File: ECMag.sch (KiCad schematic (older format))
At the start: 43 parts, among them J1 Conn_01x12, J2 Conn_01x05, J3 Conn_01x04, J4 USB_B, J5 Barrel_Jack_SW, J6 Conn_01x04, K1 Tactil Switch B3F NA, K2 Tactil Switch B3F NA, K3 Tactil Switch B3F NA, K4 Tactil Switch B3F NA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

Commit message: Rediseño de fuente step up 5v-12v y Actualizacion de datasheets
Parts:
- removed U3: XL6009, Package_TO_SOT_SMD:TO-263-5_TabPin6, symbol Enc_Mag:XL6009
- added R9: 2K2 1%, Resistor_THT:R_Axial_DIN0207_L6.3mm_D2.5mm_P7.62mm_Horizontal, symbol Enc_Mag:Resistencia
- added U3: LM2577, Package_TO_SOT_THT:TO-220-5_P3.4x3.7mm_StaggerOdd_Lead3.8mm_Vertical, symbol Enc_Mag:LM2577
- C2: value 100nF Cerámico -> 330nF Cerámico
- P1: value 10K -> 25K
- R1: value 330 1% -> 2K 1%
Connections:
- net labels added: a1, a10, a2, a3, a4, a5, a6, a7, a8, a9
- wire segments 162 -> 172
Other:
- moved on the sheet: C1, C2

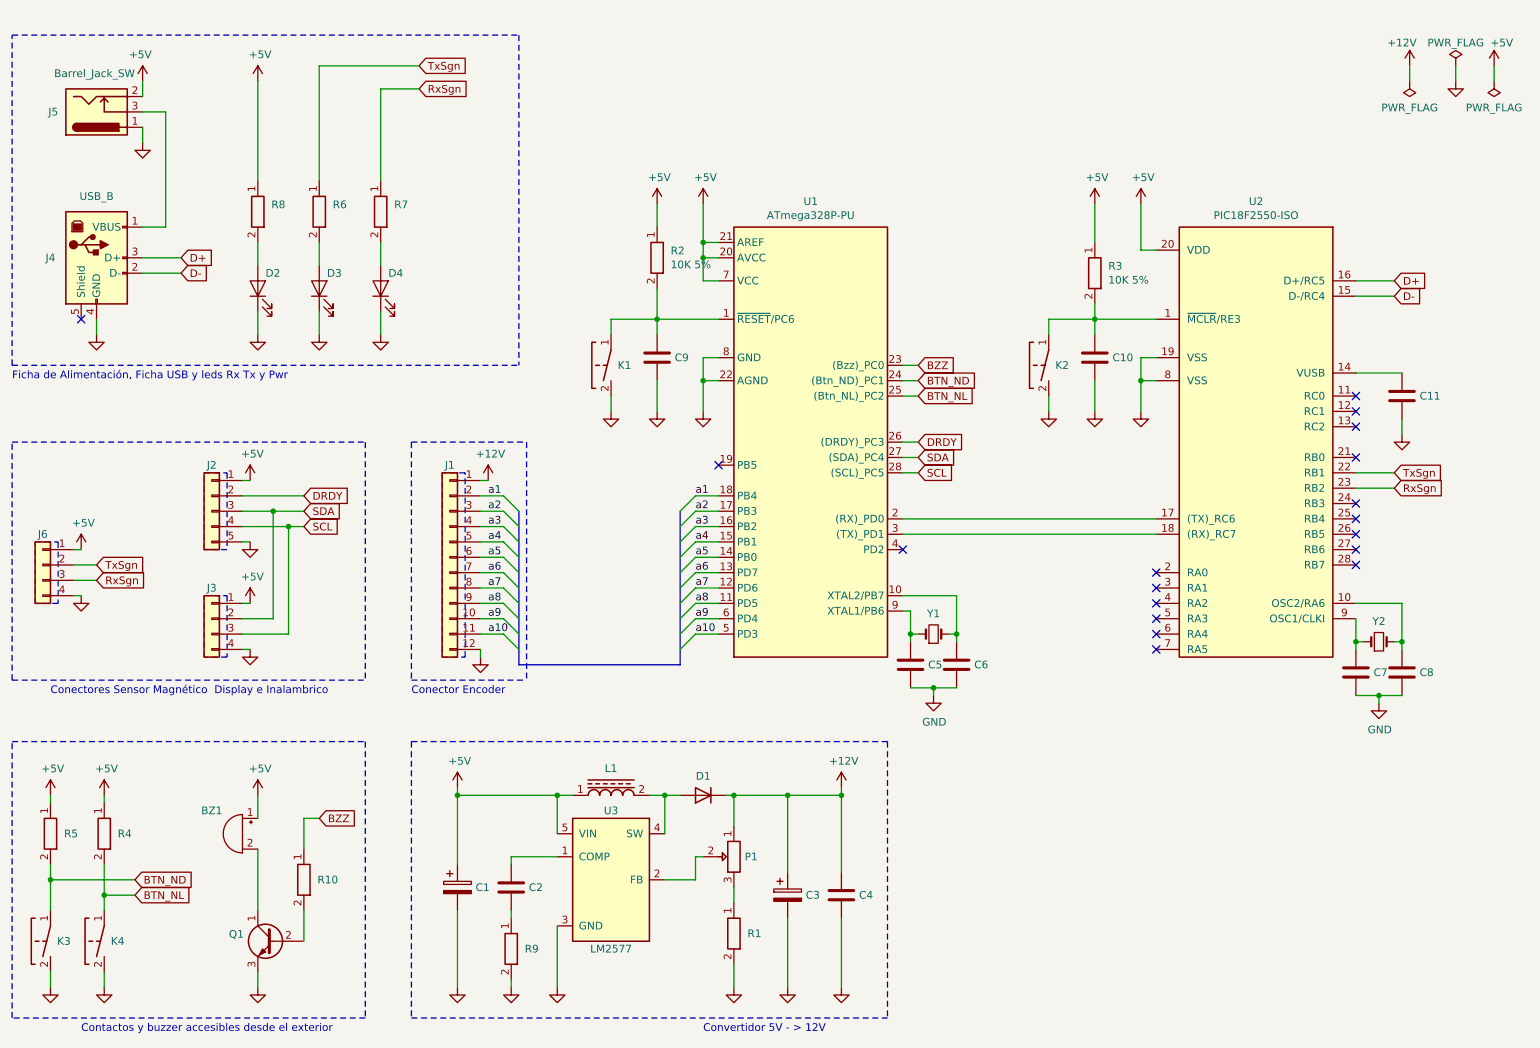
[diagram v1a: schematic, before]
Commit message: compleción de huellas faltantes y reemplazo de etiquetas por buses
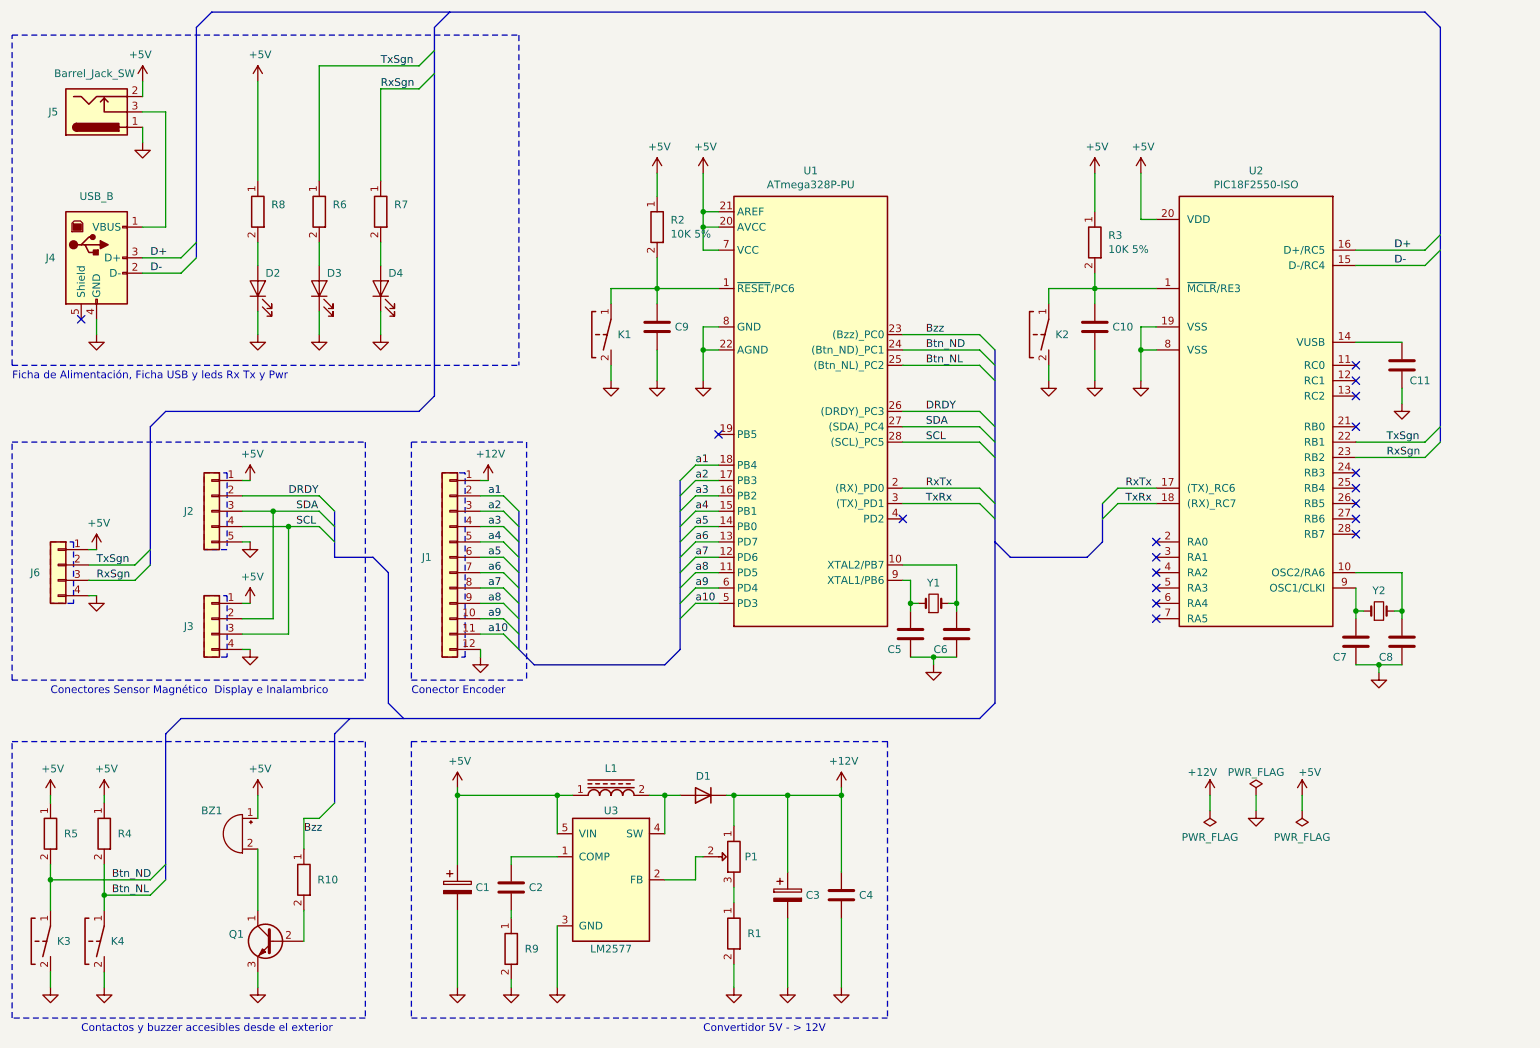
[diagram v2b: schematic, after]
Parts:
- J1: footprint (none) -> Connector_PinHeader_1.27mm:PinHeader_1x12_P1.27mm_Vertical
- J2: footprint (none) -> Connector_PinHeader_1.27mm:PinHeader_1x05_P1.27mm_Vertical
- J3, J6: footprint (none) -> Connector_PinHeader_1.27mm:PinHeader_1x04_P1.27mm_Vertical
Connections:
- net RxTx: now reaches U1.2 ((RX)_PD0), U2.17 ((TX)_RC6)
- net TxRx: now reaches U1.3 ((TX)_PD1), U2.18 ((RX)_RC7)
- net BTN_ND renamed Btn_ND
- net BTN_NL renamed Btn_NL
- net BZZ renamed Bzz
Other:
- moved on the sheet: C10, C11, C5, C6, C7, C8, C9, J6, K1, K2, R2, R3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

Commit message: Inicio de PCB
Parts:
- added H1, H2, H3, H4: MountingHole, MountingHole:MountingHole_3.2mm_M3, symbol Mechanical:MountingHole
- D1: footprint Diode_THT:D_DO-27_P15.24mm_Horizontal -> Diode_THT:D_A-405_P10.16mm_Horizontal
- U2: footprint Package_SO:SOIC-28W_7.5x17.9mm_P1.27mm -> Package_DIP:DIP-28_W7.62mm
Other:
- moved on the sheet: C10, C11, C7, C8, K2, R3, U2, Y2

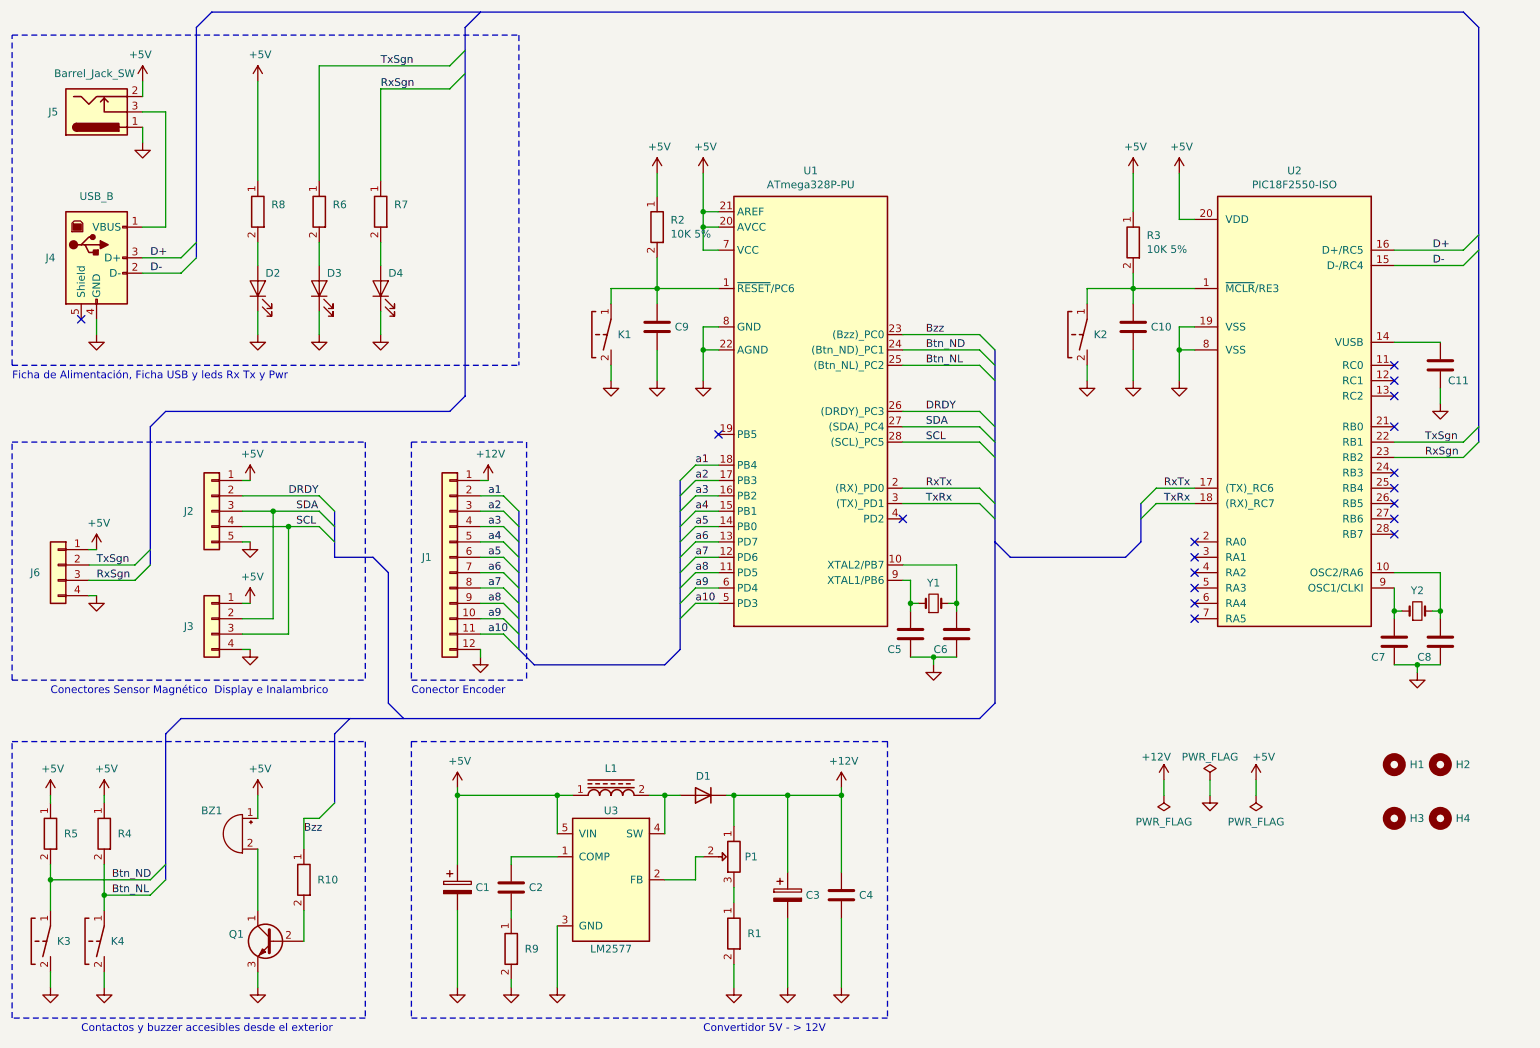
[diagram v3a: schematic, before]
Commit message: agregado de valores de los componentes en el esquemático
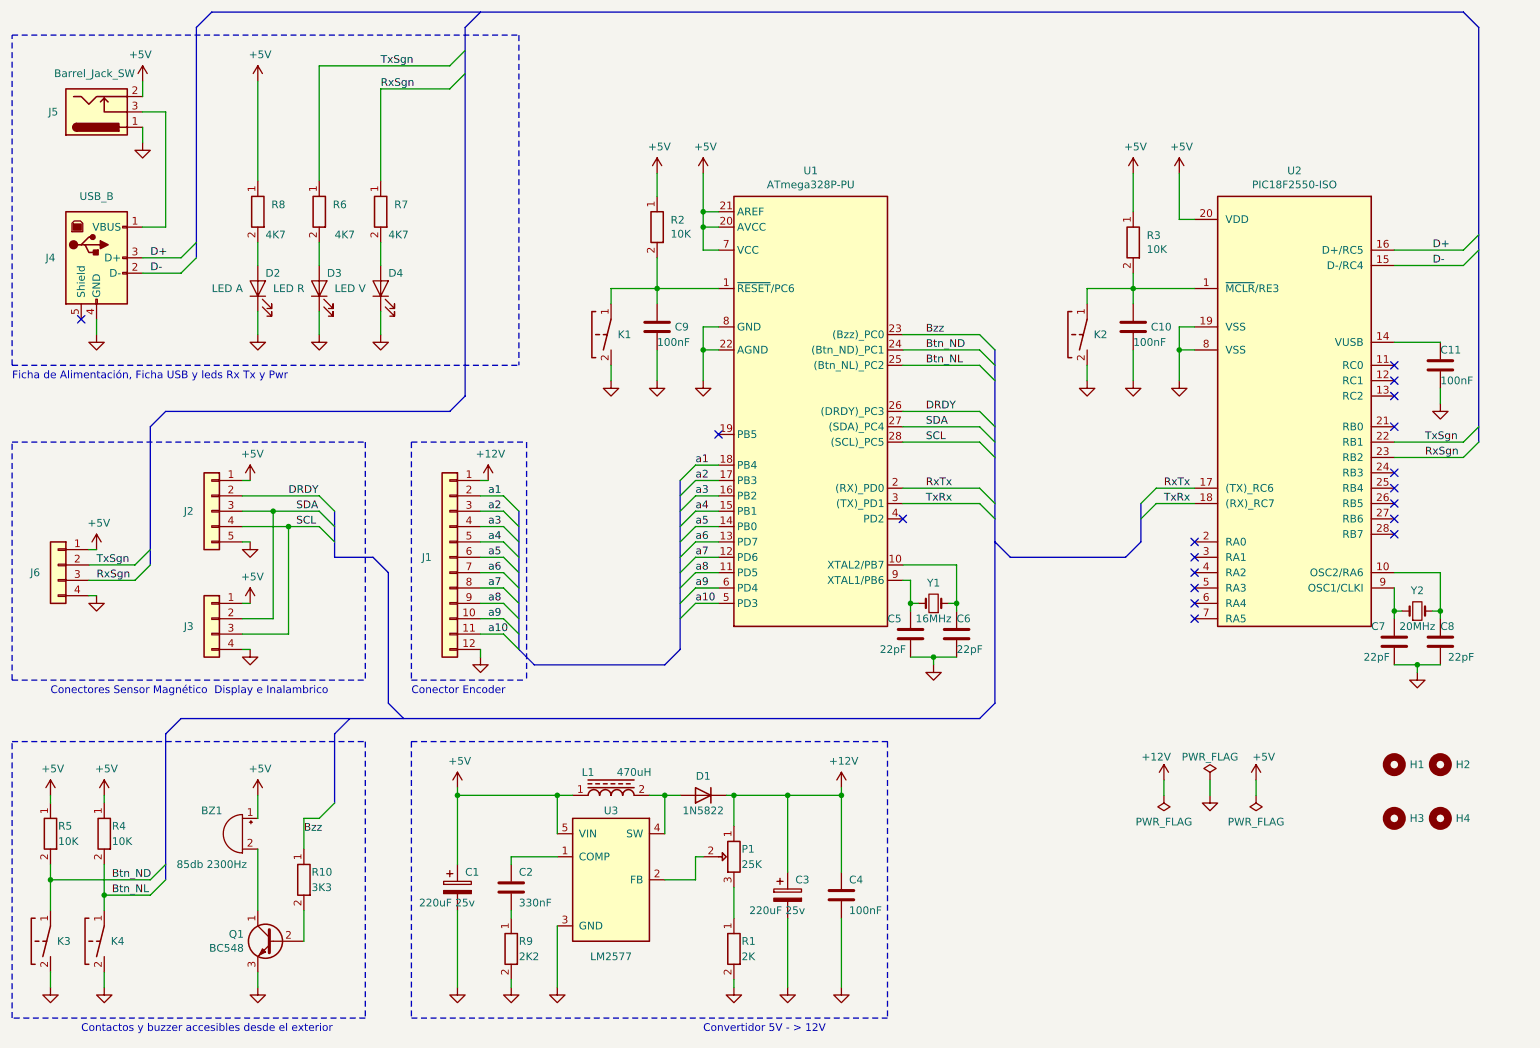
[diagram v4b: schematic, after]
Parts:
- BZ1: value Buzzer 5V 85db 2300Hz -> 85db 2300Hz
- C1, C3: value 220uF 25v HT -> 220uF 25v
- C2: value 330nF Cerámico -> 330nF
- C4: value 100nF Cerámico -> 100nF
- D2: value LED Azul -> LED A
- D3: value LED Rojo -> LED R
- D4: value LED Verde -> LED V
- J1: footprint Connector_PinHeader_1.27mm:PinHeader_1x12_P1.27mm_Vertical -> Connector_PinHeader_2.54mm:PinHeader_1x12_P2.54mm_Vertical
- J2: footprint Connector_PinHeader_1.27mm:PinHeader_1x05_P1.27mm_Vertical -> Connector_PinHeader_2.54mm:PinHeader_1x05_P2.54mm_Vertical
- J3, J6: footprint Connector_PinHeader_1.27mm:PinHeader_1x04_P1.27mm_Vertical -> Connector_PinHeader_2.54mm:PinHeader_1x04_P2.54mm_Vertical
- R1: value 2K 1% -> 2K
- R10: value 3K3 5% -> 3K3
- R2, R3, R4, R5: value 10K 5% -> 10K
- R6, R7, R8: value 4K7 5% -> 4K7
- R9: value 2K2 1% -> 2K2
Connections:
- net at C6.1, U1.10 (XTAL2/PB7): now also Y1.1; no longer Y1.2
- net at C5.1, U1.9 (XTAL1/PB6): now also Y1.2; no longer Y1.1
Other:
- moved on the sheet: R1

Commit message: Edicion de huella de pulsadores y primer pcb
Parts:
- K1, K2, K3, K4: footprint Button_Switch_THT:SW_PUSH_6mm_H5mm -> EMS_huellas:SW_6x5mm_2C
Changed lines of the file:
@@
 F 0 "K1" V 4850 2807 50  0000 R CNN
 F 1 "Tactil Switch B3F NA" V 4895 2806 50  0001 R CNN
-F 2 "Button_Switch_THT:SW_PUSH_6mm_H5mm" H 4775 3025 50  0001 C CNN
+F 2 "EMS_huellas:SW_6x5mm_2C" H 4775 3025 50  0001 C CNN
 F 3 "https://www.mouser.com/datasheet/2/307/en-b3f-13826.pdf" H 4775 3025 50  0001 C CNN
 	1    4850 2850
@@
 F 0 "K2" V 7950 2807 50  0000 R CNN
 F 1 "Tactil Switch B3F NA" V 7995 2806 50  0001 R CNN
-F 2 "Button_Switch_THT:SW_PUSH_6mm_H5mm" H 7875 3025 50  0001 C CNN
+F 2 "EMS_huellas:SW_6x5mm_2C" H 7875 3025 50  0001 C CNN
 F 3 "https://www.mouser.com/datasheet/2/307/en-b3f-13826.pdf" H 7875 3025 50  0001 C CNN
 	1    7950 2850
@@
 F 0 "K3" V 1200 6757 50  0000 R CNN
 F 1 "Tactil Switch B3F NA" V 1245 6756 50  0001 R CNN
-F 2 "Button_Switch_THT:SW_PUSH_6mm_H5mm" H 1125 6975 50  0001 C CNN
+F 2 "EMS_huellas:SW_6x5mm_2C" H 1125 6975 50  0001 C CNN
 F 3 "https://www.mouser.com/datasheet/2/307/en-b3f-13826.pdf" H 1125 6975 50  0001 C CNN
 	1    1200 6800
@@
 F 0 "K4" V 1550 6757 50  0000 R CNN
 F 1 "Tactil Switch B3F NA" V 1595 6756 50  0001 R CNN
-F 2 "Button_Switch_THT:SW_PUSH_6mm_H5mm" H 1475 6975 50  0001 C CNN
+F 2 "EMS_huellas:SW_6x5mm_2C" H 1475 6975 50  0001 C CNN
 F 3 "https://www.mouser.com/datasheet/2/307/en-b3f-13826.pdf" H 1475 6975 50  0001 C CNN
 	1    1550 6800
